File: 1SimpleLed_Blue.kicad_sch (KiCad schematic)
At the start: 10 parts, among them J1 JST_SH_SM06B-SRSS-TB_1x06-1MP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, J4 Conn_01x04, Q1 BSS84, U1 M24C02-FMN

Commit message: Change I2C pull-up resistors value to 4.7K
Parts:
- R5, R6: value 2.2K -> 4.7K
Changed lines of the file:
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@@
 			)
 		)
-		(property "Value" "2.2K"
+		(property "Value" "4.7K"
 			(at 38.1 84.836 90)
 			(effects
@@
 			)
 		)
-		(property "Value" "2.2K"
+		(property "Value" "4.7K"
 			(at 38.1 94.488 90)
 			(effects

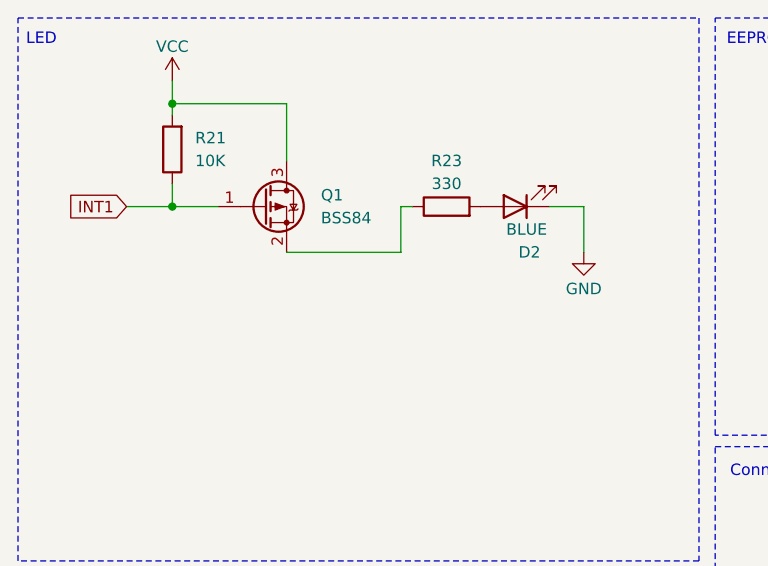
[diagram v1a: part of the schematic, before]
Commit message: Fix the design around MOSFET and add resistor in series to protect MCU's GPIO line
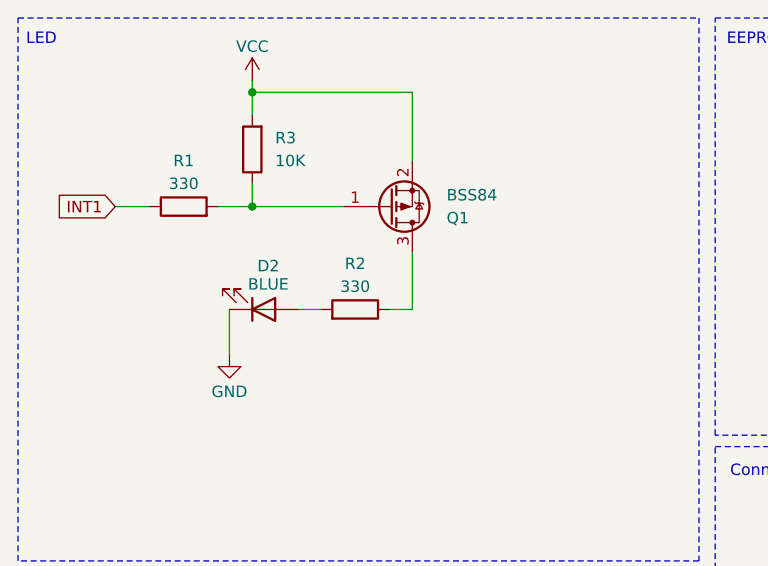
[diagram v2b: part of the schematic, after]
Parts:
- added R1: 330, Resistor_SMD:R_0603_1608Metric, symbol Device:R
- renumbered R23 to R2, R21 to R3
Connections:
- net INT1: now also R1.1; no longer Q1.1 (G), R3.1
- net VCC: now also Q1.2 (S); no longer Q1.3 (D)
- net at R2.1: now also Q1.3 (D); no longer Q1.2 (S)
- new net: Q1.1 (G), R1.2, R3.1
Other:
- moved on the sheet: D2, Q1, R2, R3
